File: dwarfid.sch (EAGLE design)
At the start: 17 parts, among them Q1 mmbt3904, Q4 mmbt3906, Q5 mmbt3906

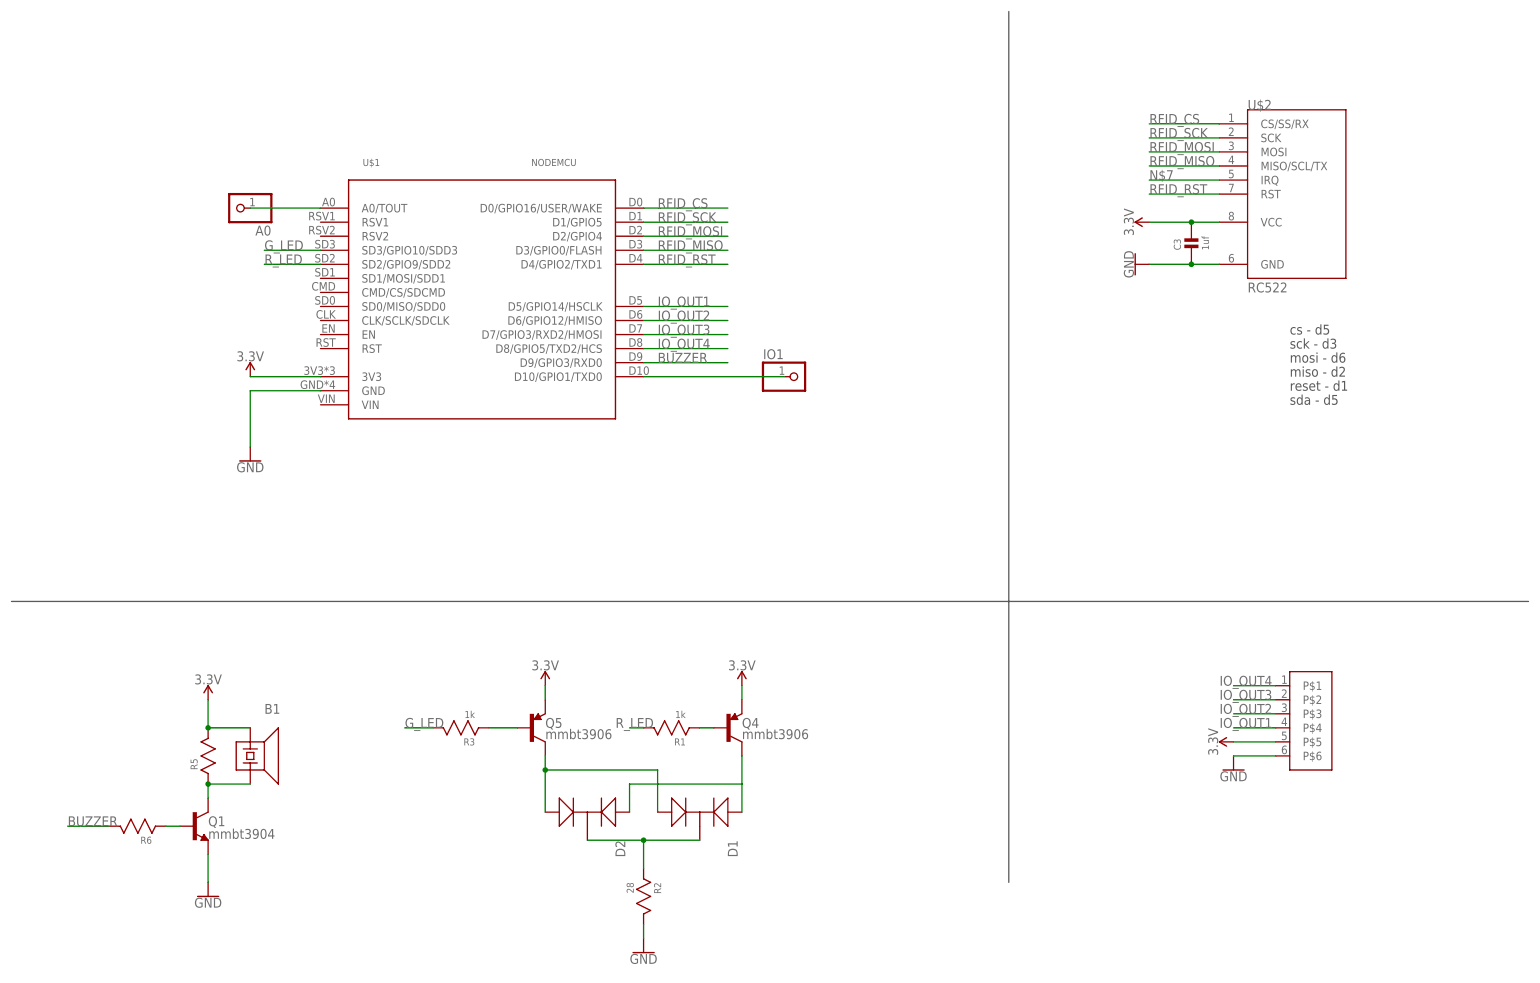
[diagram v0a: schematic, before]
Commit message: fixed the spacing for the nodeMCU pins
moved the LEDs to the bottom of the display

Changed the current setting resistor for both the LEDs and the buzzer to 100 ohms.

remapped the rfid card reader to use pins that can also be used as hardware spi pins.

Put both the buzzer and the LEDs on pwm compatible pins

replaced the 6pin jst connector with an 8pin connector.

added the other hardware spi pins to the jst connector.
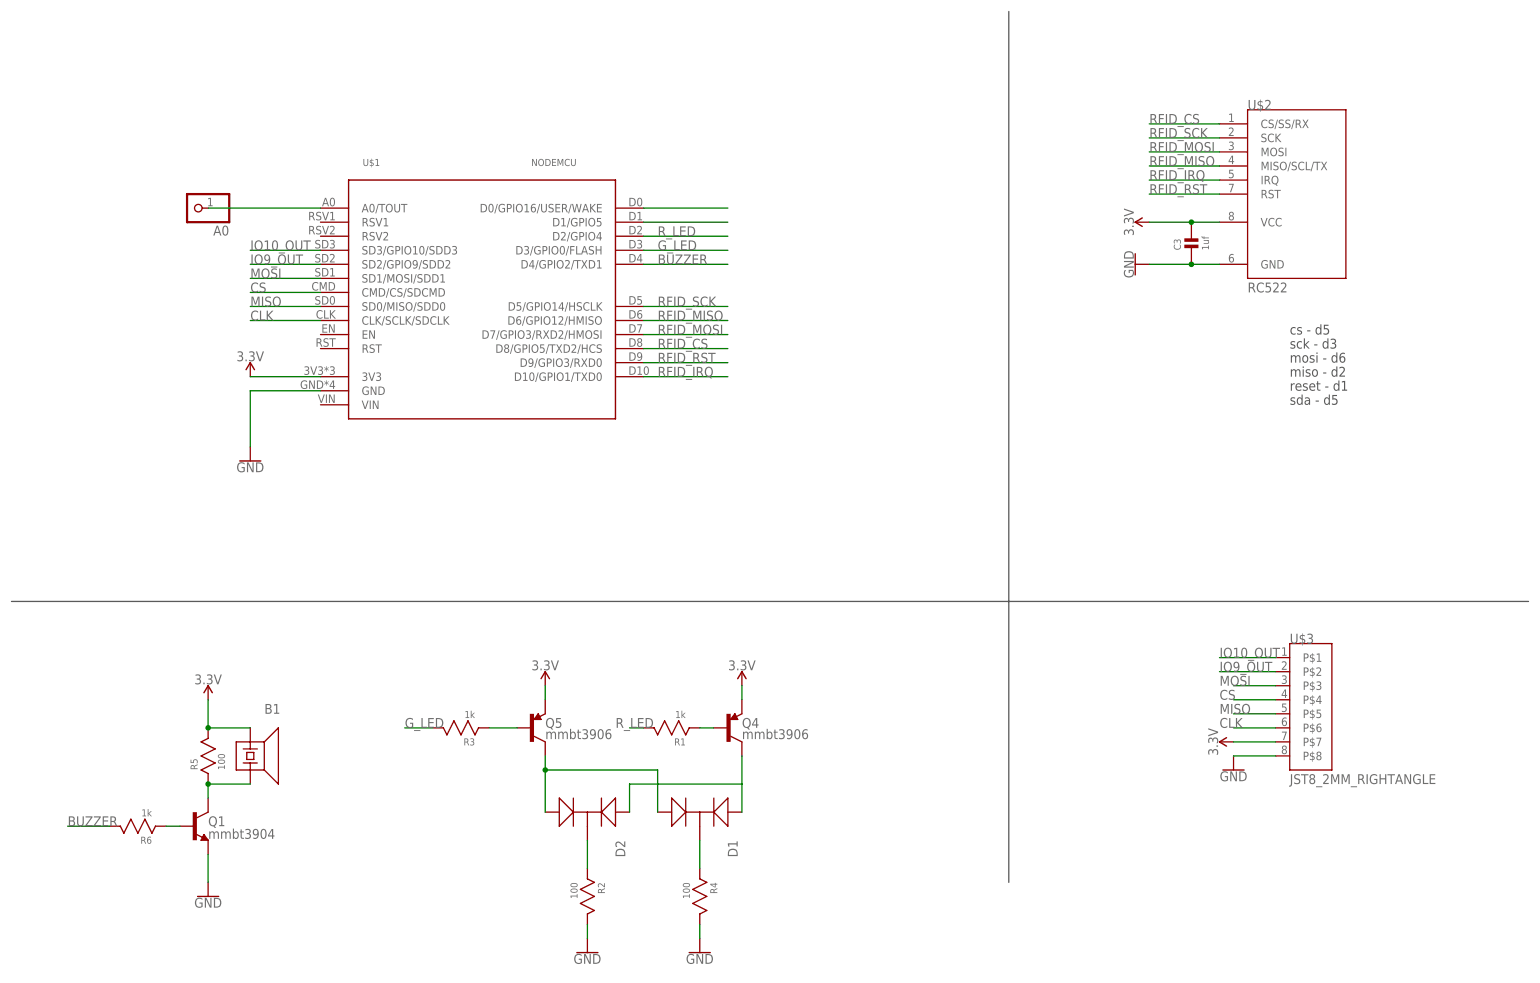
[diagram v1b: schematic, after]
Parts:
- removed IO1: (no value), adafruit:PINHD-1X1
- removed U$5: JST6_2MM_RIGHTANGLE, rowe_connectors:JST6_2MM_RIGHTANGLE
- added R4: 100, rowe_passives:RES_0603
- added U$3: JST8_2MM_RIGHTANGLE, rowe_connectors:JST8_2MM_RIGHTANGLE
- R2: value 28 -> 100
- R5: value (none) -> 100
- R6: value (none) -> 1k
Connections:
- removed net IO_OUT1: U$1.D5/GPIO14/HSCLK, U$5.P$4
- removed net IO_OUT2: U$1.D6/GPIO12/HMISO, U$5.P$3
- removed net IO_OUT3: U$1.D7/GPIO3/RXD2/HMOSI, U$5.P$2
- removed net IO_OUT4: U$1.D8/GPIO5/TXD2/HCS, U$5.P$1
- removed net N$10: IO1.1, U$1.D10/GPIO1/TXD0
- removed net N$7: U$2.IRQ
- new net CLK: U$1.CLK/SCLK/SDCLK, U$3.P$6
- new net CS: U$1.CMD/CS/SDCMD, U$3.P$4
- new net IO10_OUT: U$1.SD3/GPIO10/SDD3, U$3.P$1
- new net IO9_OUT: U$1.SD2/GPIO9/SDD2, U$3.P$2
- new net MISO: U$1.SD0/MISO/SDD0, U$3.P$5
- new net MOSI: U$1.SD1/MOSI/SDD1, U$3.P$3
- new net N$11: D1.2, R4.P$1
- new net N$12: U$1.D1/GPIO5
- new net N$13: U$1.D0/GPIO16/USER/WAKE
- new net RFID_IRQ: U$1.D10/GPIO1/TXD0, U$2.IRQ
- net 3.3V: now also U$3.P$7; no longer U$5.P$5
- net BUZZER: now also U$1.D4/GPIO2/TXD1; no longer U$1.D9/GPIO3/RXD0
- net GND: now also R4.P$2, U$3.P$8; no longer U$5.P$6
- net G_LED: now also U$1.D3/GPIO0/FLASH; no longer U$1.SD3/GPIO10/SDD3
- net N$1: no longer D1.2
- net RFID_CS: now also U$1.D8/GPIO5/TXD2/HCS; no longer U$1.D0/GPIO16/USER/WAKE
- net RFID_MISO: now also U$1.D6/GPIO12/HMISO; no longer U$1.D3/GPIO0/FLASH
- net RFID_MOSI: now also U$1.D7/GPIO3/RXD2/HMOSI; no longer U$1.D2/GPIO4
- net RFID_RST: now also U$1.D9/GPIO3/RXD0; no longer U$1.D4/GPIO2/TXD1
- net RFID_SCK: now also U$1.D5/GPIO14/HSCLK; no longer U$1.D1/GPIO5
- net R_LED: now also U$1.D2/GPIO4; no longer U$1.SD2/GPIO9/SDD2
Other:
- moved on the sheet: A0, R2

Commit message: minor intermediate changed before switching out the LEDs for
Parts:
- R5: value 100 -> 1k
- R6: value 1k -> 100
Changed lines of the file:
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@@
 <part name="B1" library="rowe_actuators" library_urn="urn:adsk.eagle:library:493550" deviceset="PS1720P02_PIEZO_BUZZER" device="" package3d_urn="urn:adsk.eagle:package:493553/3"/>
 <part name="Q1" library="SparkFun-DiscreteSemi" deviceset="TRANS_NPN" device="-MMBT2222AL" value="mmbt3904"/>
-<part name="R5" library="rowe_passives" library_urn="urn:adsk.eagle:library:487190" deviceset="RES_0603" device="" package3d_urn="urn:adsk.eagle:package:487200/4" value="100"/>
-<part name="R6" library="rowe_passives" library_urn="urn:adsk.eagle:library:487190" deviceset="RES_0603" device="" package3d_urn="urn:adsk.eagle:package:487200/4" value="1k"/>
+<part name="R5" library="rowe_passives" library_urn="urn:adsk.eagle:library:487190" deviceset="RES_0603" device="" package3d_urn="urn:adsk.eagle:package:487200/4" value="1k"/>
+<part name="R6" library="rowe_passives" library_urn="urn:adsk.eagle:library:487190" deviceset="RES_0603" device="" package3d_urn="urn:adsk.eagle:package:487200/4" value="100"/>
 <part name="GND3" library="SparkFun-PowerSymbols" deviceset="GND" device=""/>
 <part name="SUPPLY3" library="SparkFun-PowerSymbols" deviceset="3.3V" device=""/>

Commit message: replaced the LEDs with WS2812Bs.
Moved the rfid board down so that it will be easier to solder.

unfortunately both of these changes required us to increase the size of the board.
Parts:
- removed D1, D2: (no value), rowe_actuators:WP59EGW
- removed Q4, Q5: mmbt3906, SparkFun-DiscreteSemi:TRANS_PNP-PMBT3906|MMBT3906L
- removed R1, R3: 1k, rowe_passives:RES_0603
- removed R2, R4: 100, rowe_passives:RES_0603
- added C1, C2: 100nf, rowe_passives:CAP_0603
- added D3, D4: WS2812B, rowe_actuators:WS2812B
- added LDOUT: (no value), adafruit:PINHD-1X1
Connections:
- removed net G_LED: R3.P$2, U$1.D3/GPIO0/FLASH
- removed net N$1: D2.2, R2.P$1
- removed net N$11: D1.2, R4.P$1
- removed net N$12: U$1.D1/GPIO5
- removed net N$13: U$1.D0/GPIO16/USER/WAKE
- removed net N$3: D1.1, D2.1, Q4.C
- removed net N$4: Q5.B, R3.P$1
- removed net N$5: D1.3, D2.3, Q5.C
- removed net R_LED: R1.P$2, U$1.D2/GPIO4
- new net LIGHT_DIN: D3.DIN, U$1.D3/GPIO0/FLASH
- new net N$7: D3.DOUT, D4.DIN
- net 3.3V: now also C1.P$2, C2.P$2, D3.VDD, D4.VDD; no longer Q4.E, Q5.E
- net GND: now also C1.P$1, C2.P$1, D3.VSS, D4.VSS; no longer R2.P$2, R4.P$2
- net N$2: now also D4.DOUT, LDOUT.1; no longer Q4.B, R1.P$1
- net RFID_CS: now also U$1.D8/GPIO15/TXD2/HCS; no longer U$1.D8/GPIO5/TXD2/HCS
- net RFID_MOSI: now also U$1.D7/GPIO13/RXD2/HMOSI; no longer U$1.D7/GPIO3/RXD2/HMOSI
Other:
- note removed: "cs - d5"
- note removed: "miso - d2"
- note removed: "mosi - d6"
- note removed: "reset - d1"
- note removed: "sck - d3"
- note removed: "sda - d5"
